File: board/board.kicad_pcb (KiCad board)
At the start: 2 copper layers, 45 x 29 mm, 38 parts, among them J1 019_100BASE-T_with_CT, J2 LPJ4265BDNL, U1 LD39200PU33R, U2 MP8007, U3 POE30P-50L

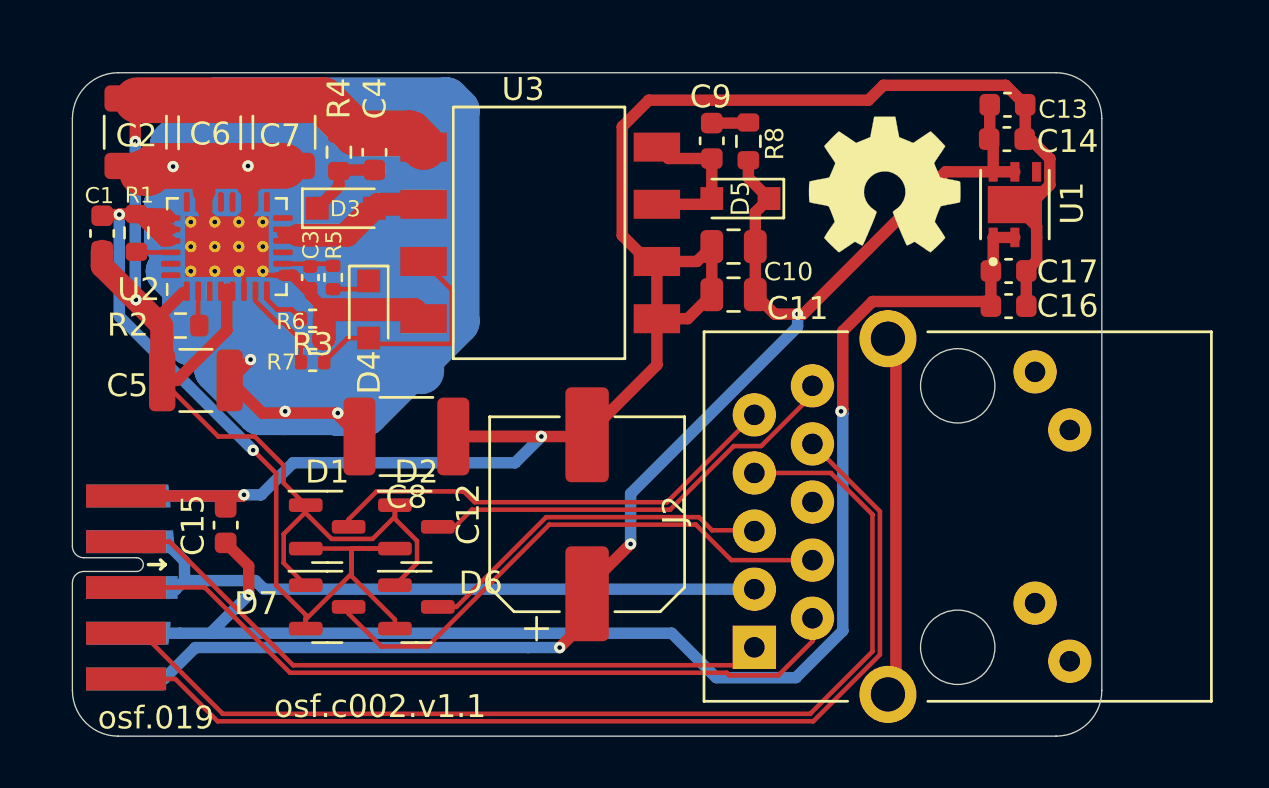
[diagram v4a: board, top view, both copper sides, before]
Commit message: added pours for LDO and LCSC parts
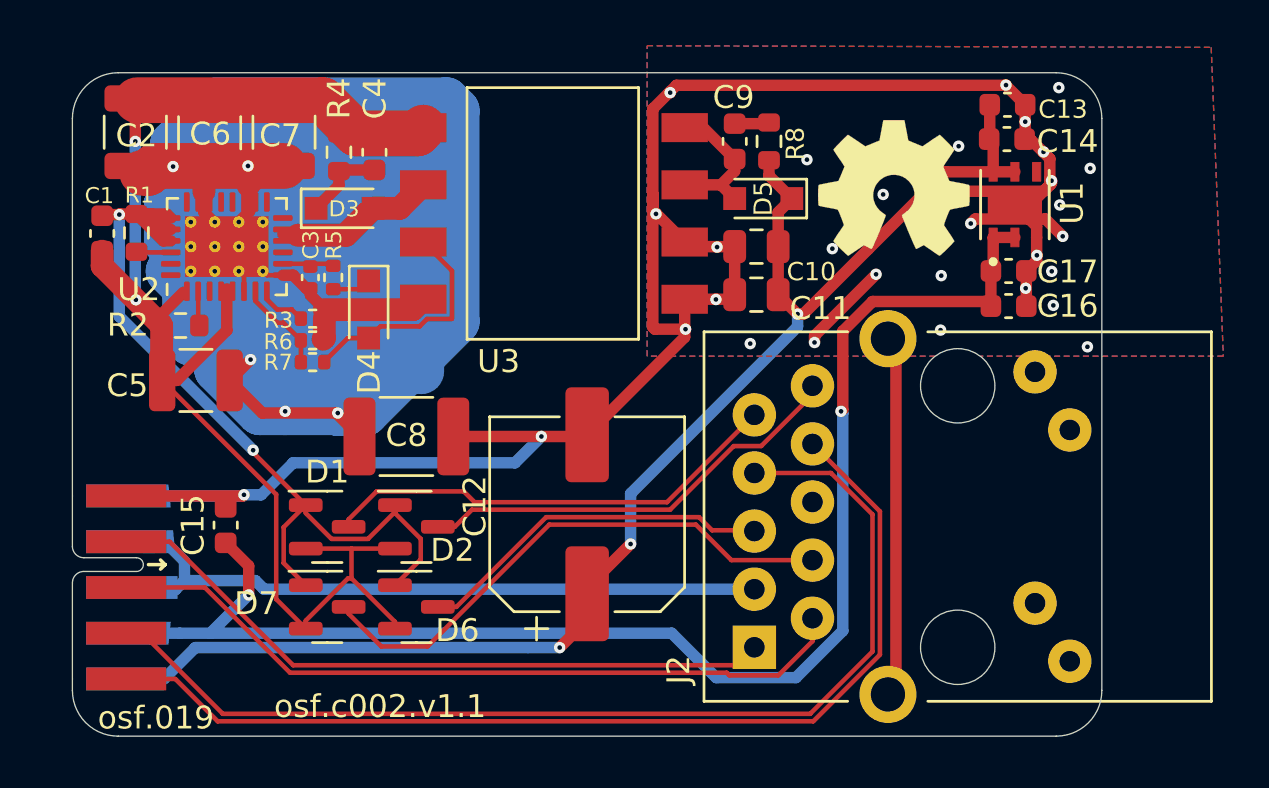
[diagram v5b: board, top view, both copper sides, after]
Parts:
- C1: value 100n -> 100nF
- C9: value 10n -> 10nF
- moved U3 1.04 mm to (161.1, 80.2)
- moved C9 1.00 mm to (168.9, 77.0)
- moved C10 1.00 mm to (169.9, 81.6)
- moved C11 1.00 mm to (169.9, 83.7)
- moved D5 1.00 mm to (170.2, 79.5)
- moved R8 0.90 mm to (170.4, 77.0)
- moved LOGO1 0.43 mm to (175.9, 79.0)
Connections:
- D1 pad 1: /Controller/PoE+ -> /Controller/PoE-
- D1 pad 2: /Controller/PoE- -> /Controller/PoE+
- D2 pad 1: /Controller/PoE+ -> /Controller/PoE-
- D2 pad 2: /Controller/PoE- -> /Controller/PoE+
- D6 pad 1: /Controller/PoE+ -> /Controller/PoE-
- D6 pad 2: /Controller/PoE- -> /Controller/PoE+
- D7 pad 1: /Controller/PoE+ -> /Controller/PoE-
- D7 pad 2: /Controller/PoE- -> /Controller/PoE+
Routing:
- net GND: track 87.0 -> 99.5 mm, vias 2 -> 32
- net /Controller/PoE-: track 42.8 -> 37.2 mm
- net /Controller/PoE+: track 64.2 -> 65.6 mm
- net /Controller/5V: track 62.2 -> 61.3 mm
- added copper zone on B.Cu, net GND
- added copper zone on F.Cu, net GND
